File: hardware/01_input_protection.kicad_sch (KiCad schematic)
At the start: 5 parts, among them J1 USB4105-GF-A, U1 CH224A

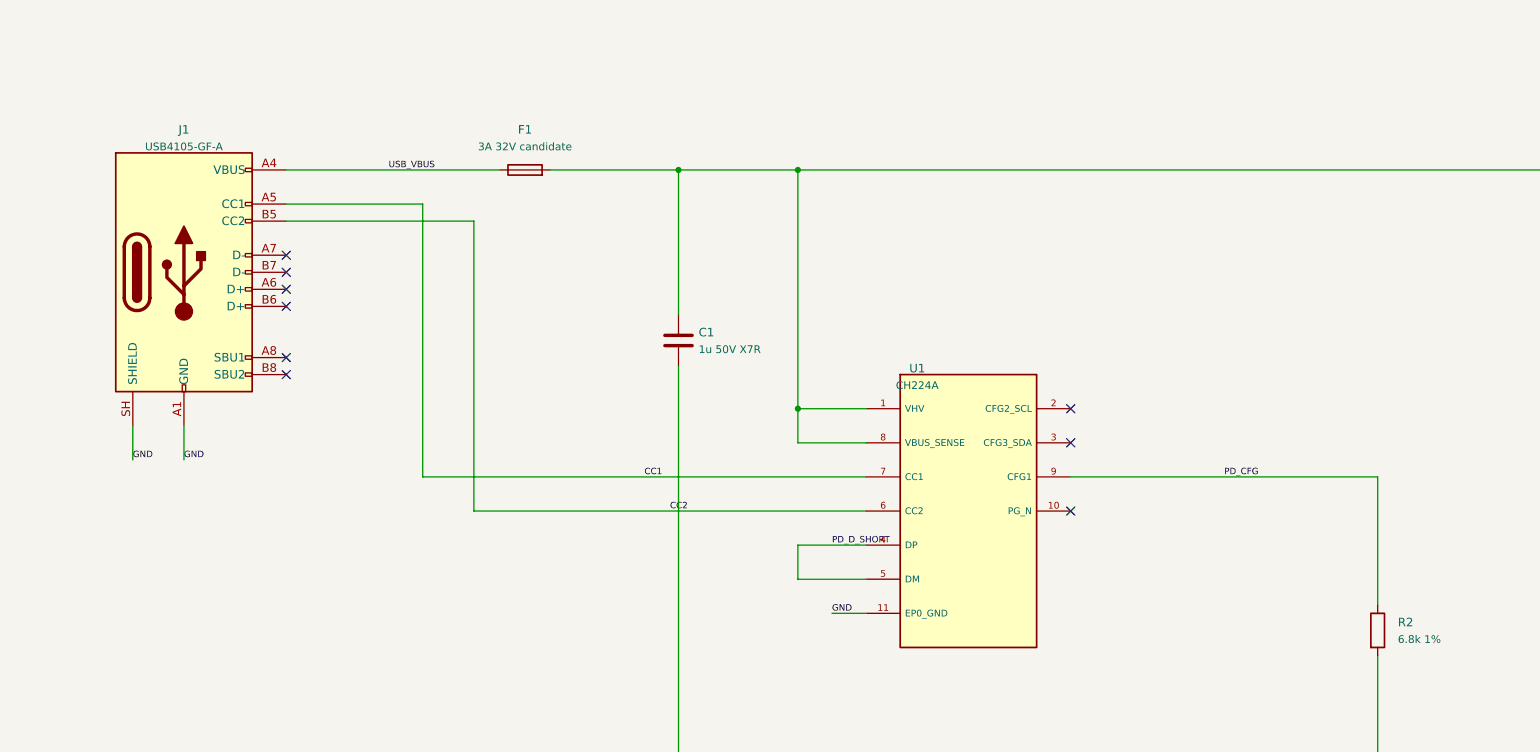
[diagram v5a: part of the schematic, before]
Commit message: Complete four-layer routing, adopt proven HRO USB-C and release checked fabrication files
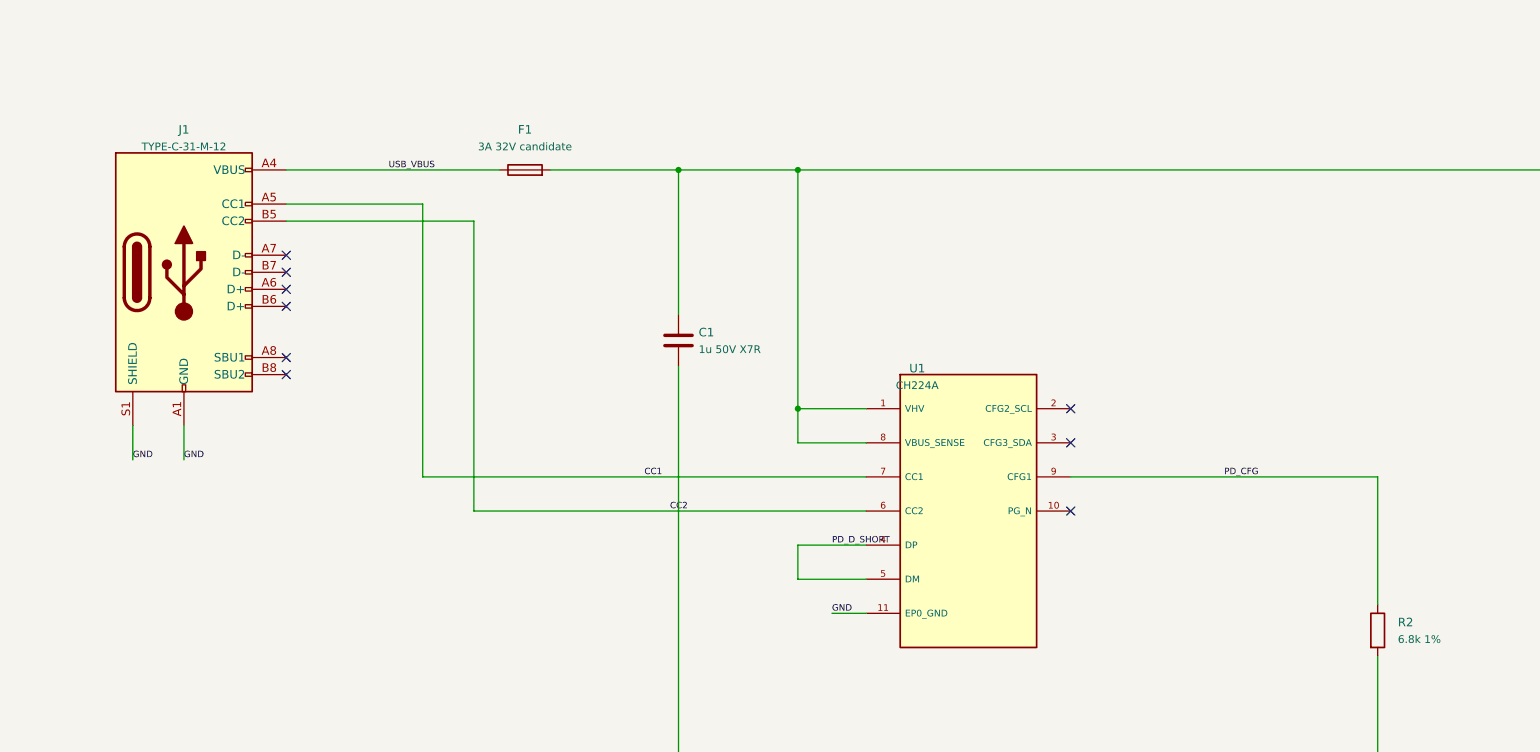
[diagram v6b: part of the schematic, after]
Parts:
- J1: value USB4105-GF-A -> TYPE-C-31-M-12; footprint BigModular:USB_C_Receptacle_GCT_USB4105-xx-A_16P_TopMnt_Horizontal -> BigModular:HRO-TYPE-C-31-M-12; symbol BigModular:Connector_USB_C_Receptacle_USB2.0_16P -> BigModular:HRO_TYPE_C_31_M_12; LCSC (none) -> C165948; MPN USB4105-GF-A -> TYPE-C-31-M-12; Manufacturer (none) -> HRO (Korean Hroparts Elec); NOTE Prototype candidate; qualify ratings, land pattern and oper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 -> HRO C165948; Bread local land. A1 includes B12; A4 includes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
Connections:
- net GND: now also J1.S1 (SHIELD); no longer J1.B1 (GND), J1.B12 (GND), J1.SH (SHIELD)
- net USB_VBUS: no longer J1.B4 (VBUS), J1.B9 (VBUS)

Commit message: Use standard vias and front-only Economy assembly with Basic passive networks and DNP LED
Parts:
- C1: LCSC (none) -> C28323; MPN (none) -> CL21B105KBFNNNE; Manufacturer (none) -> Samsung Electro-Mechanics
- J1: JLCPCB Audit Requirements {"assembly": "manual", "reason": "User-selected manual inte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 -> {"assembly": "jlcpcb", "reason": "Economy catalog candidate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; JLCPCB Exclude yes -> no; NOTE HRO C165948; Bread local land. A1 includes B12; A4 includes B9; A9 includes B4; A12 includes B1; S1 shell=GND. USB data/SBU NC. No verified 3D model; see docs/usb-hro-review.md. -> HRO C165948; Bread local land. A1 includes B12; A4 includes B9; A9 includes B4; A12 includes B1; S1 shell=GND. USB data/SBU NC. No verified 3D model; see docs/usb-hro-review.md. Economy catalog candidate; front SMT contacts with four plated shell slots requiring explicit supplier solder-process review; not quote approval.
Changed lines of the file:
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@@
 		)
 	)
-	(symbol
-		(lib_id "BigModular:Device_C")
-		(at 119.38 91.44 0)
-		(unit 1)
-		(body_style 1)
-		(exclude_from_sim no)
-		(in_bom yes)
-		(on_board yes)
-		(in_pos_files yes)
-		(dnp no)
-		(property "Reference" "C1"
-			(at 122.38 90.24 0)
-			(show_name no)
-			(do_not_autoplace no)
-			(effects
-				(font
-					(size 1.27 1.27)
-				)
-				(justify left)
-			)
-		)
-		(property "Value" "1u 50V X7R"
-			(at 122.38 92.78 0)
-			(show_name no)
-			(do_not_autoplace no)
-			(effects
-				(font
-					(size 1.15 1.15)
-				)
-				(justify left)
-			)
-		)
-		(property "Footprint" "BigModular:C_0805_2012Metric"
-			(at 119.38 91.44 0)
-			(hide yes)
-			(show_name no)
-			(do_not_autoplace no)
-			(effects
-				(font
-					(size 1 1)
-				)
-			)
-		)
-		(property "Datasheet" ""
-			(at 119.38 91.44 0)
-			(hide yes)
-			(show_name no)
-			(do_not_autoplace no)
-			(effects
-				(font
-					(size 1 1)
-				)
-			)
-		)
-		(property "Description" ""
-			(at 119.38 91.44 0)
-			(show_name no)
-			(do_not_autoplace no)
-			(effects
-				(font
-					(size 1.27 1.27)
-				)
-			)
-		)
-		(property "MPN" ""
-			(at 119.38 91.44 0)
-			(hide yes)
-			(show_name no)
-			(do_not_autoplace no)
-			(effects
-				(font
-					(size 1 1)
-				)
-			)
-		)
-		(property "LCSC" ""
-			(at 119.38 91.44 0)
-			(hide yes)
-			(show_name no)
-			(do_not_autoplace no)
-			(effects
-				(font
-					(size 1 1)
-				)
-			)
-		)
-		(property "NOTE" "Effective capacitance under DC bias and temperature must be verified; no automatic reuse approval."
-			(at 119.38 91.44 0)
-			(hide yes)
-			(show_name no)
-			(do_not_autoplace no)
-			(effects
-				(font
-					(size 1 1)
-				)
-			)
-		)
-		(property "JLCPCB Exclude" "no"
-			(at 119.38 91.44 0)
-			(hide yes)
-			(show_name no)
-			(do_not_autoplace no)
-			(effects
-				(font
-					(size 1 1)
-				)
-			)
-		)
-		(property "JLCPCB Audit Requirements" "{}"
-			(at 119.38 91.44 0)
-			(hide yes)
-			(show_name no)
-			(do_not_autoplace no)
-			(effects
-				(font
-					(size 1 1)
-				)
-			)
-		)
-		(pin "1"
-		)
-		(pin "2"
-		)
-		(instances
-			(project "big_modular"
-				(path "/d567704c-57ad-5df1-b183-cadb01fd8972/3f5b5140-2fea-5c66-ba3b-ec707e3f47f1"
-					(reference "C1")
-					(unit 1)
-				)
-			)
-		)
-	)
-	(symbol (lib_id "BigModular:HRO_TYPE_C_31_M_12") (at 45.72 81.28 0) (unit 1) (body_style 1) (exclude_from_sim no) (in_bom yes) (on_board yes) (in_pos_files yes) (dnp no) (property "Reference" "J1" (at 45.72 60.04 0) (show_name no) (do_not_autoplace no) (effects (font (size 1.27 1.27)))) (property "Value" "TYPE-C-31-M-12" (at 45.72 62.58 0) (show_name no) (do_not_autoplace no) (effects (font (size 1.15 1.15)))) (property "Footprint" "BigModular:HRO-TYPE-C-31-M-12" (at 45.72 81.28 0) (hide yes) (show_name no) (do_not_autoplace no) (effects (font (size 1 1)))) (property "Datasheet" "https://datasheet.lcsc.com/datasheet/pdf/9e56b777c022540fcce7c7f67825f55e.pdf?productCode=C165948" (at 45.72 81.28 0) (hide yes) (show_name no) (do_not_autoplace no) (effects (font (size 1 1)))) (property "Description" "" (at 45.72 81.28 0) (show_name no) (do_not_autoplace no) (effects (font (size 1.27 1.27)))) (property "MPN" "TYPE-C-31-M-12" (at 45.72 81.28 0) (hide yes) (show_name no) (do_not_autoplace no) (effects (font (size 1 1)))) (property "LCSC" "C165948" (at 45.72 81.28 0) (hide yes) (show_name no) (do_not_autoplace no) (effects (font (size 1 1)))) (property "NOTE" "HRO C165948; Bread local land. A1 includes B12; A4 includes B9; A9 includes B4; A12 includes B1; S1 shell=GND. USB data/SBU NC. No verified 3D model; see docs/usb-hro-review.md." (at 45.72 81.28 0) (hide yes) (show_name no) (do_not_autoplace no) (effects (font (size 1 1)))) (property "JLCPCB Exclude" "yes" (at 45.72 81.28 0) (hide yes) (show_name no) (do_not_autoplace no) (effects (font (size 1 1)))) (property "JLCPCB Audit Requirements" "{\"assembly\": \"manual\", \"reason\": \"User-selected manual interface/LED, excluded from JLC placement.\"}" (at 45.72 81.28 0) (hide yes) (show_name no) (do_not_autoplace no) (effects (font (size 1 1)))) (pin "A1") (pin "A4") (pin "A5") (pin "A6") (pin "A7") (pin "A8") (pin "A9") (pin "A12") (pin "B5") (pin "B6") (pin "B7") (pin "B8") (pin "S1") (instances (project "big_modular" (path "/d567704c-57ad-5df1-b183-cadb01fd8972/3f5b5140-2fea-5c66-ba3b-ec707e3f47f1" (reference "J1") (unit 1)))) (property "Manufacturer" "HRO (Korean Hroparts Elec)" (at 45.72 62.58 0) (show_name no) (do_not_autoplace no) (effects (font (size 1.15 1.15)) hide)))
+	(symbol (lib_id "BigModular:Device_C") (at 119.38 91.44 0) (unit 1) (body_style 1) (exclude_from_sim no) (in_bom yes) (on_board yes) (in_pos_files yes) (dnp no) (property "Reference" "C1" (at 122.38 90.24 0) (show_name no) (do_not_autoplace no) (effects (font (size 1.27 1.27)) (justify left))) (property "Value" "1u 50V X7R" (at 122.38 92.78 0) (show_name no) (do_not_autoplace no) (effects (font (size 1.15 1.15)) (justify left))) (property "Footprint" "BigModular:C_0805_2012Metric" (at 119.38 91.44 0) (hide yes) (show_name no) (do_not_autoplace no) (effects (font (size 1 1)))) (property "Datasheet" "https://www.lcsc.com/datasheet/lcsc_datasheet_2304140030_Samsung-Electro-Mechanics-CL21B105KBFNNNE_C28323.pdf" (at 119.38 91.44 0) (hide yes) (show_name no) (do_not_autoplace no) (effects (font (size 1 1)))) (property "Description" "" (at 119.38 91.44 0) (show_name no) (do_not_autoplace no) (effects (font (size 1.27 1.27)))) (property "MPN" "CL21B105KBFNNNE" (at 119.38 91.44 0) (hide yes) (show_name no) (do_not_autoplace no) (effects (font (size 1 1)))) (property "LCSC" "C28323" (at 119.38 91.44 0) (hide yes) (show_name no) (do_not_autoplace no) (effects (font (size 1 1)))) (property "NOTE" "Effective capacitance under DC bias and temperature must be verified; no automatic reuse approval." (at 119.38 91.44 0) (hide yes) (show_name no) (do_not_autoplace no) (effects (font (size 1 1)))) (property "JLCPCB Exclude" "no" (at 119.38 91.44 0) (hide yes) (show_name no) (do_not_autoplace no) (effects (font (size 1 1)))) (property "JLCPCB Audit Requirements" "{}" (at 119.38 91.44 0) (hide yes) (show_name no) (do_not_autoplace no) (effects (font (size 1 1)))) (pin "1") (pin "2") (instances (project "big_modular" (path "/d567704c-57ad-5df1-b183-cadb01fd8972/3f5b5140-2fea-5c66-ba3b-ec707e3f47f1" (reference "C1") (unit 1)))) (property "Manufacturer" "Samsung Electro-Mechanics" (at 122.38 92.78 0) (show_name no) (do_not_autoplace no) (effects (font (size 1.15 1.15)) (justify left) hide)))
+	(symbol (lib_id "BigModular:HRO_TYPE_C_31_M_12") (at 45.72 81.28 0) (unit 1) (body_style 1) (exclude_from_sim no) (in_bom yes) (on_board yes) (in_pos_files yes) (dnp no) (property "Reference" "J1" (at 45.72 60.04 0) (show_name no) (do_not_autoplace no) (effects (font (size 1.27 1.27)))) (property "Value" "TYPE-C-31-M-12" (at 45.72 62.58 0) (show_name no) (do_not_autoplace no) (effects (font (size 1.15 1.15)))) (property "Footprint" "BigModular:HRO-TYPE-C-31-M-12" (at 45.72 81.28 0) (hide yes) (show_name no) (do_not_autoplace no) (effects (font (size 1 1)))) (property "Datasheet" "https://datasheet.lcsc.com/datasheet/pdf/9e56b777c022540fcce7c7f67825f55e.pdf?productCode=C165948" (at 45.72 81.28 0) (hide yes) (show_name no) (do_not_autoplace no) (effects (font (size 1 1)))) (property "Description" "" (at 45.72 81.28 0) (show_name no) (do_not_autoplace no) (effects (font (size 1.27 1.27)))) (property "MPN" "TYPE-C-31-M-12" (at 45.72 81.28 0) (hide yes) (show_name no) (do_not_autoplace no) (effects (font (size 1 1)))) (property "LCSC" "C165948" (at 45.72 81.28 0) (hide yes) (show_name no) (do_not_autoplace no) (effects (font (size 1 1)))) (property "NOTE" "HRO C165948; Bread local land. A1 includes B12; A4 includes B9; A9 includes B4; A12 includes B1; S1 shell=GND. USB data/SBU NC. No verified 3D model; see docs/usb-hro-review.md. Economy catalog candidate; front SMT contacts with four plated shell slots requiring explicit supplier solder-process review; not quote approval." (at 45.72 81.28 0) (hide yes) (show_name no) (do_not_autoplace no) (effects (font (size 1 1)))) (property "JLCPCB Exclude" "no" (at 45.72 81.28 0) (hide yes) (show_name no) (do_not_autoplace no) (effects (font (size 1 1)))) (property "JLCPCB Audit Requirements" "{\"assembly\": \"jlcpcb\", \"reason\": \"Economy catalog candidate; supplier process/preview approval pending.\"}" (at 45.72 81.28 0) (hide yes) (show_name no) (do_not_autoplace no) (effects (font (size 1 1)))) (pin "A1") (pin "A4") (pin "A5") (pin "A6") (pin "A7") (pin "A8") (pin "A9") (pin "A12") (pin "B5") (pin "B6") (pin "B7") (pin "B8") (pin "S1") (instances (project "big_modular" (path "/d567704c-57ad-5df1-b183-cadb01fd8972/3f5b5140-2fea-5c66-ba3b-ec707e3f47f1" (reference "J1") (unit 1)))) (property "Manufacturer" "HRO (Korean Hroparts Elec)" (at 45.72 62.58 0) (show_name no) (do_not_autoplace no) (effects (font (size 1.15 1.15)) hide)))
 	(symbol
 		(lib_id "BigModular:power_PWR_FLAG")
